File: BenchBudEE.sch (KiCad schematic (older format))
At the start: 0 parts

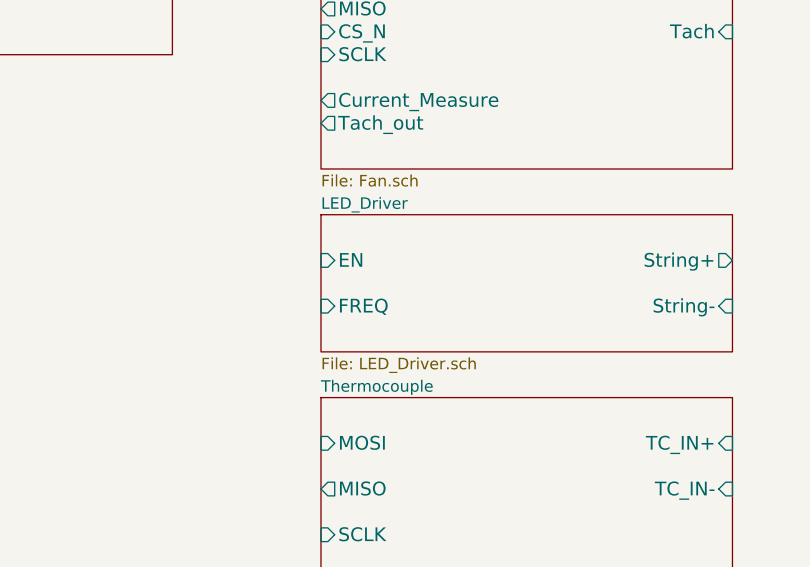
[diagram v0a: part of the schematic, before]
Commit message: Rough schematic created for LED driver circuit
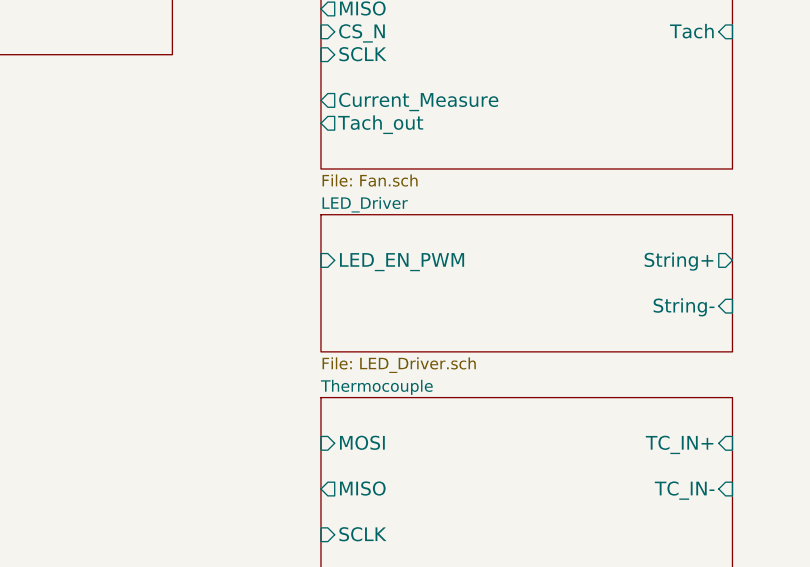
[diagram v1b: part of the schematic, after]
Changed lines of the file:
@@
 F0 "LED_Driver" 50
 F1 "LED_Driver.sch" 50
-F2 "EN" I L 7500 3300 60
-F3 "FREQ" I L 7500 3500 60
-F4 "String+" O R 9300 3300 60
-F5 "String-" I R 9300 3500 60
+F2 "String+" O R 9300 3300 60
+F3 "String-" I R 9300 3500 60
+F4 "LED_EN_PWM" I L 7500 3300 60
 $EndSheet
 $Sheet

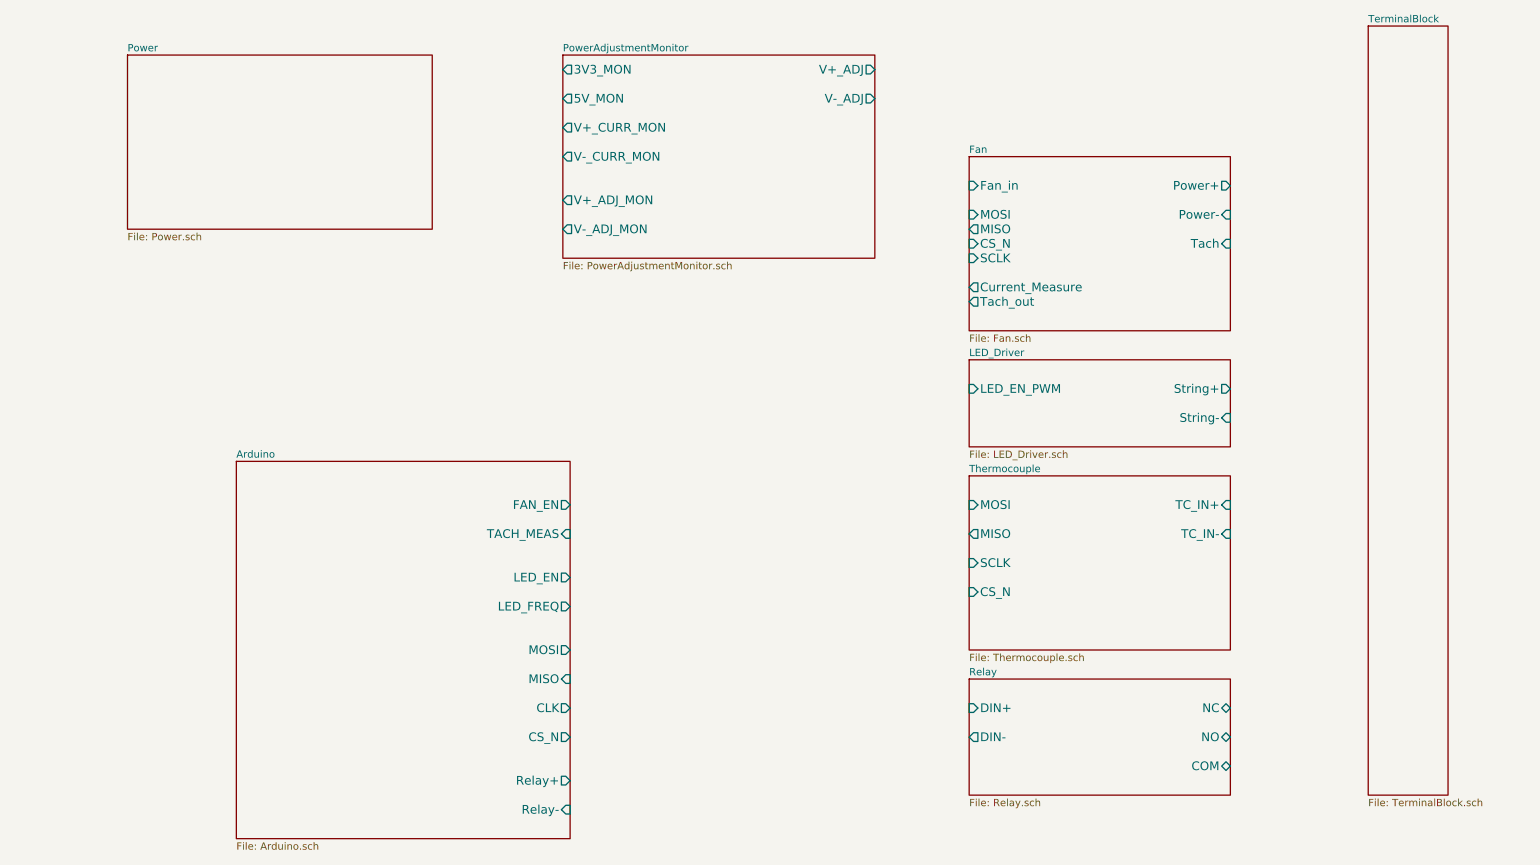
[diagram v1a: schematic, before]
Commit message: Added Arduino and top-level connections
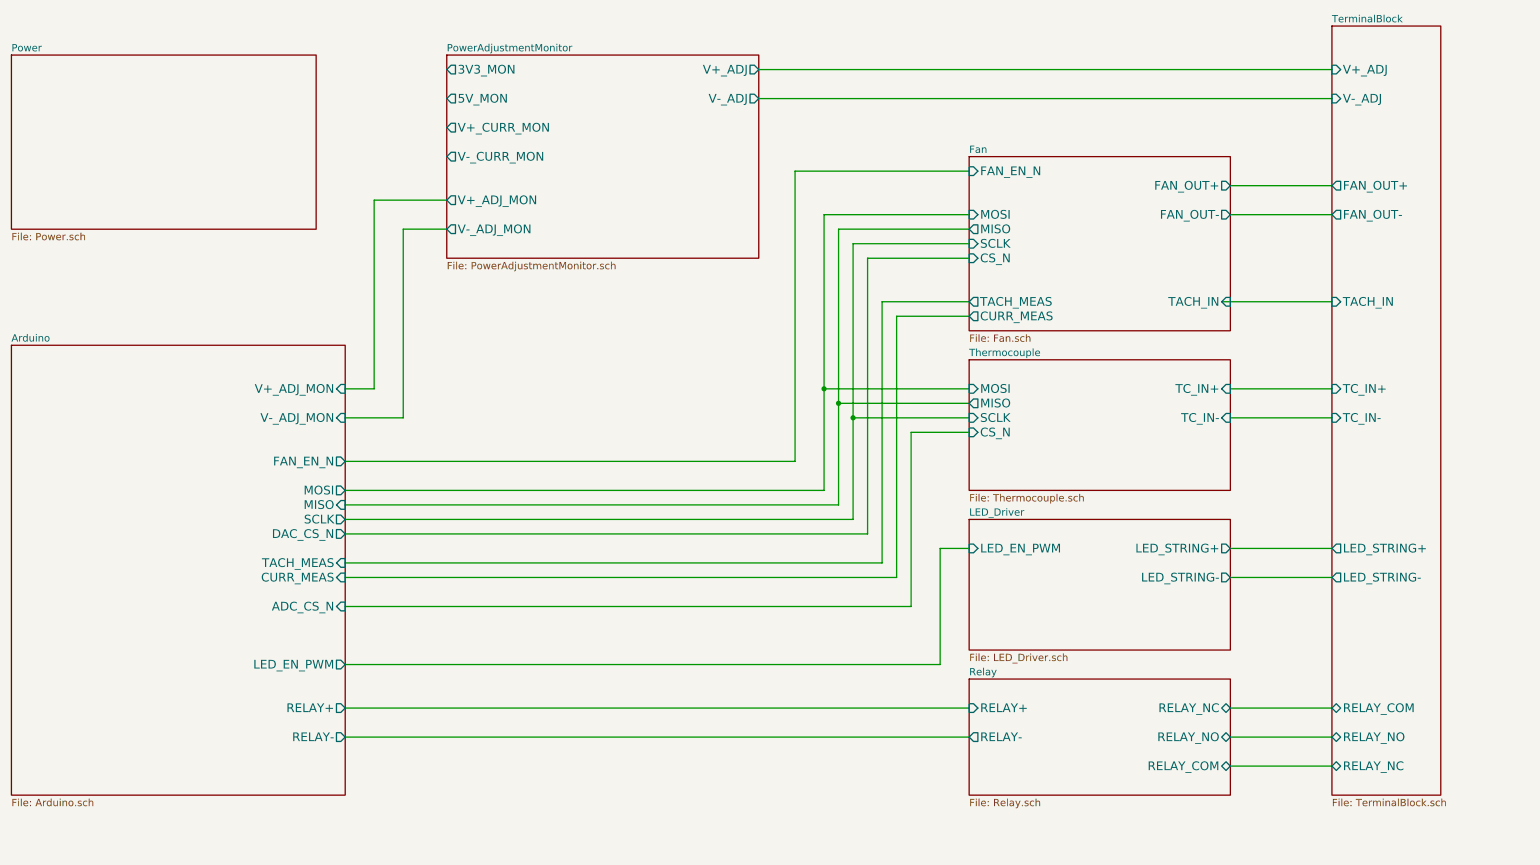
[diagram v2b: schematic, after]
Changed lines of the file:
@@
 $EndDescr
-$Sheet
-S 7500 3900 1800 1200
-U 52EAE493
-F0 "Thermocouple" 50
-F1 "Thermocouple.sch" 50
-F2 "TC_IN+" I R 9300 4100 60
-F3 "TC_IN-" I R 9300 4300 60
-F4 "MOSI" I L 7500 4100 60
-F5 "MISO" O L 7500 4300 60
-F6 "SCLK" I L 7500 4500 60
-F7 "CS_N" I L 7500 4700 60
-$EndSheet
 $Sheet
 S 7500 5300 1800 800
@@
 F0 "Relay" 50
 F1 "Relay.sch" 50
-F2 "DIN+" I L 7500 5500 60
-F3 "DIN-" O L 7500 5700 60
-F4 "NC" B R 9300 5500 60
-F5 "NO" B R 9300 5700 60
-F6 "COM" B R 9300 5900 60
-$EndSheet
-$Sheet
-S 7500 3100 1800 600
+F4 "RELAY_NC" B R 9300 5500 60
+F5 "RELAY_NO" B R 9300 5700 60
+F6 "RELAY_COM" B R 9300 5900 60
+F7 "RELAY+" I L 7500 5500 60
+F8 "RELAY-" O L 7500 5700 60
+$EndSheet
+$Sheet
+S 7500 4200 1800 900
 U 52EAE512
 F0 "LED_Driver" 50
 F1 "LED_Driver.sch" 50
-F2 "String+" O R 9300 3300 60
-F3 "String-" I R 9300 3500 60
-F4 "LED_EN_PWM" I L 7500 3300 60
-$EndSheet
-$Sheet
-S 1700 1000 2100 1200
+F2 "LED_EN_PWM" I L 7500 4400 60
+F3 "LED_STRING+" O R 9300 4400 60
+F4 "LED_STRING-" O R 9300 4600 60
+$EndSheet
+$Sheet
+S 900  1000 2100 1200
 U 52EAE4E0
 F0 "Power" 50
@@
 $EndSheet
 $Sheet
-S 10250 800  550  5300
+S 10000 800  750  5300
 U 52EAE551
 F0 "TerminalBlock" 50
 F1 "TerminalBlock.sch" 50
-$EndSheet
-$Sheet
-S 2450 3800 2300 2600
-U 52EAE42B
-F0 "Arduino" 50
-F1 "Arduino.sch" 50
-F2 "Relay+" O R 4750 6000 60
-F3 "Relay-" I R 4750 6200 60
-F4 "MOSI" O R 4750 5100 60
-F5 "MISO" I R 4750 5300 60
-F6 "CLK" O R 4750 5500 60
-F7 "CS_N" O R 4750 5700 60
-F8 "LED_EN" O R 4750 4600 60
-F9 "LED_FREQ" O R 4750 4800 60
-F10 "FAN_EN" O R 4750 4100 60
-F11 "TACH_MEAS" I R 4750 4300 60
-$EndSheet
+F2 "V+_ADJ" I L 10000 1100 60
+F3 "V-_ADJ" I L 10000 1300 60
+F4 "FAN_OUT+" O L 10000 1900 60
+F5 "FAN_OUT-" O L 10000 2100 60
+F6 "TACH_IN" I L 10000 2700 60
+F7 "LED_STRING+" O L 10000 4400 60
+F8 "LED_STRING-" O L 10000 4600 60
+F9 "TC_IN+" I L 10000 3300 60
+F10 "TC_IN-" I L 10000 3500 60
+F11 "RELAY_COM" B L 10000 5500 60
+F12 "RELAY_NO" B L 10000 5700 60
+F13 "RELAY_NC" B L 10000 5900 60
+$EndSheet
+$Sheet
+S 3900 1000 2150 1400
+U 52F17012
+F0 "PowerAdjustmentMonitor" 50
+F1 "PowerAdjustmentMonitor.sch" 50
+F2 "V+_ADJ" O R 6050 1100 60
+F3 "V-_ADJ" O R 6050 1300 60
+F4 "3V3_MON" O L 3900 1100 60
+F5 "5V_MON" O L 3900 1300 60
+F6 "V+_ADJ_MON" O L 3900 2000 60
+F7 "V-_ADJ_MON" O L 3900 2200 60
+F8 "V+_CURR_MON" O L 3900 1500 60
+F9 "V-_CURR_MON" O L 3900 1700 60
+$EndSheet
+Wire Wire Line
+	10000 1100 6050 1100
+Wire Wire Line
+	10000 1300 6050 1300
+Wire Wire Line
+	10000 1900 9300 1900
+Wire Wire Line
+	10000 2100 9300 2100
+Wire Wire Line
+	9250 2700 10000 2700
+Wire Wire Line
+	10000 3300 9300 3300
+Wire Wire Line
+	10000 3500 9300 3500
+Wire Wire Line
+	10000 4400 9300 4400
+Wire Wire Line
+	10000 4600 9300 4600
+Wire Wire Line
+	10000 5500 9300 5500
+Wire Wire Line
+	10000 5700 9300 5700
+Wire Wire Line
+	10000 5900 9300 5900
+Wire Wire Line
+	3200 3300 3400 3300
+Wire Wire Line
+	3400 3300 3400 2000
+Wire Wire Line
+	3400 2000 3900 2000
+Wire Wire Line
+	3200 3500 3600 3500
+Wire Wire Line
+	3600 3500 3600 2200
+Wire Wire Line
+	3600 2200 3900 2200
+Wire Wire Line
+	3200 3800 6300 3800
+Wire Wire Line
+	6300 3800 6300 1800
+Wire Wire Line
+	6300 1800 7500 1800
+Wire Wire Line
+	6500 4000 3200 4000
+Wire Wire Line
+	6500 2100 6500 4000
+Wire Wire Line
+	6500 2100 7500 2100
+Wire Wire Line
+	6600 4100 3200 4100
+Wire Wire Line
+	6600 2200 6600 4100
+Wire Wire Line
+	6600 2200 7500 2200
+Wire Wire Line
+	6700 4200 3200 4200
+Wire Wire Line
+	6700 2300 6700 4200
+Wire Wire Line
+	6700 2300 7500 2300
+Wire Wire Line
+	3200 4300 6800 4300
+Wire Wire Line
+	6800 4300 6800 2400
+Wire Wire Line
+	6800 2400 7500 2400
+Wire Wire Line
+	3200 4500 6900 4500
+Wire Wire Line
+	6900 4500 6900 2700
+Wire Wire Line
+	6900 2700 7500 2700
+Wire Wire Line
+	3200 4600 7000 4600
+Wire Wire Line
+	7000 4600 7000 2800
+Wire Wire Line
+	7000 2800 7500 2800
 $Sheet
 S 7500 1700 1800 1200
@@
 F0 "Fan" 50
 F1 "Fan.sch" 50
-F2 "Power+" O R 9300 1900 60
-F3 "Power-" I R 9300 2100 60
-F4 "Tach" I R 9300 2300 60
-F5 "Tach_out" O L 7500 2700 60
-F6 "Fan_in" I L 7500 1900 60
-F7 "Current_Measure" O L 7500 2600 60
-F8 "MOSI" I L 7500 2100 60
-F9 "MISO" O L 7500 2200 60
-F10 "CS_N" I L 7500 2300 60
-F11 "SCLK" I L 7500 2400 60
-$EndSheet
-$Sheet
-S 4700 1000 2150 1400
-U 52F17012
-F0 "PowerAdjustmentMonitor" 50
-F1 "PowerAdjustmentMonitor.sch" 50
-F2 "V+_ADJ" O R 6850 1100 60
-F3 "V-_ADJ" O R 6850 1300 60
-F4 "3V3_MON" O L 4700 1100 60
-F5 "5V_MON" O L 4700 1300 60
-F6 "V+_ADJ_MON" O L 4700 2000 60
-F7 "V-_ADJ_MON" O L 4700 2200 60
-F8 "V+_CURR_MON" O L 4700 1500 60
-F9 "V-_CURR_MON" O L 4700 1700 60
-$EndSheet
+F2 "MOSI" I L 7500 2100 60
+F3 "MISO" O L 7500 2200 60
+F4 "CS_N" I L 7500 2400 60
+F5 "SCLK" I L 7500 2300 60
+F6 "FAN_OUT+" O R 9300 1900 60
+F7 "TACH_IN" I R 9300 2700 60
+F8 "TACH_MEAS" O L 7500 2700 60
+F9 "FAN_EN_N" I L 7500 1800 60
+F10 "CURR_MEAS" O L 7500 2800 60
+F11 "FAN_OUT-" O R 9300 2100 60
+$EndSheet
+$Sheet
+S 7500 3100 1800 900
+U 52EAE493
+F0 "Thermocouple" 50
+F1 "Thermocouple.sch" 50
+F2 "TC_IN+" I R 9300 3300 60
+F3 "TC_IN-" I R 9300 3500 60
+F4 "MOSI" I L 7500 3300 60
+F5 "MISO" O L 7500 3400 60
+F6 "SCLK" I L 7500 3500 60
+F7 "CS_N" I L 7500 3600 60
+$EndSheet
+$Sheet
+S 900  3000 2300 3100
+U 52EAE42B
+F0 "Arduino" 50
+F1 "Arduino.sch" 50
+F2 "MOSI" O R 3200 4000 60
+F3 "MISO" I R 3200 4100 60
+F4 "TACH_MEAS" I R 3200 4500 60
+F5 "SCLK" O R 3200 4200 60
+F6 "FAN_EN_N" O R 3200 3800 60
+F7 "CURR_MEAS" I R 3200 4600 60
+F8 "RELAY+" O R 3200 5500 60
+F9 "RELAY-" O R 3200 5700 60
+F10 "V+_ADJ_MON" I R 3200 3300 60
+F11 "V-_ADJ_MON" I R 3200 3500 60
+F12 "LED_EN_PWM" O R 3200 5200 60
+F13 "DAC_CS_N" O R 3200 4300 60
+F14 "ADC_CS_N" I R 3200 4800 60
+$EndSheet
+Wire Wire Line
+	3200 4800 7100 4800
+Wire Wire Line
+	7100 4800 7100 3600
+Wire Wire Line
+	7100 3600 7500 3600
+Wire Wire Line
+	7500 3500 6700 3500
+Connection ~ 6700 3500
+Wire Wire Line
+	7500 3400 6600 3400
+Connection ~ 6600 3400
+Wire Wire Line
+	7500 3300 6500 3300
+Connection ~ 6500 3300
+Wire Wire Line
+	3200 5200 7300 5200
+Wire Wire Line
+	7300 5200 7300 4400
+Wire Wire Line
+	7300 4400 7500 4400
+Wire Wire Line
+	3200 5500 7500 5500
+Wire Wire Line
+	7500 5700 3200 5700
 $EndSCHEMATC

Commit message: Some cleanup/fixes on the top-level
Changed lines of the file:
@@
 	10000 5900 9300 5900
 Wire Wire Line
-	3200 3300 3400 3300
+	3200 3200 3400 3200
 Wire Wire Line
-	3400 3300 3400 2000
+	3400 3200 3400 2000
 Wire Wire Line
 	3400 2000 3900 2000
 Wire Wire Line
-	3200 3500 3600 3500
+	3200 3400 3600 3400
 Wire Wire Line
-	3600 3500 3600 2200
+	3600 3400 3600 2200
 Wire Wire Line
 	3600 2200 3900 2200
@@
 	3200 3800 6300 3800
 Wire Wire Line
-	6300 3800 6300 1800
+	6300 3800 6300 1900
 Wire Wire Line
-	6300 1800 7500 1800
+	6300 1900 7500 1900
 Wire Wire Line
 	6500 4000 3200 4000
 Wire Wire Line
-	6500 2100 6500 4000
+	6500 2100 6500 3300
+Wire Wire Line
+	6500 3300 6500 4000
 Wire Wire Line
 	6500 2100 7500 2100
@@
 	6600 4100 3200 4100
 Wire Wire Line
-	6600 2200 6600 4100
+	6600 2200 6600 3400
+Wire Wire Line
+	6600 3400 6600 4100
 Wire Wire Line
 	6600 2200 7500 2200
@@
 	6700 4200 3200 4200
 Wire Wire Line
-	6700 2300 6700 4200
+	6700 2300 6700 3500
+Wire Wire Line
+	6700 3500 6700 4200
 Wire Wire Line
 	6700 2300 7500 2300
@@
 F7 "TACH_IN" I R 9300 2700 60
 F8 "TACH_MEAS" O L 7500 2700 60
-F9 "FAN_EN_N" I L 7500 1800 60
-F10 "CURR_MEAS" O L 7500 2800 60
-F11 "FAN_OUT-" O R 9300 2100 60
+F9 "CURR_MEAS" O L 7500 2800 60
+F10 "FAN_OUT-" O R 9300 2100 60
+F11 "FAN_PWM" I L 7500 1900 60
+F12 "FAN_MODE" I L 7500 1800 60
 $EndSheet
 $Sheet
@@
 F4 "TACH_MEAS" I R 3200 4500 60
 F5 "SCLK" O R 3200 4200 60
-F6 "FAN_EN_N" O R 3200 3800 60
-F7 "CURR_MEAS" I R 3200 4600 60
-F8 "RELAY+" O R 3200 5500 60
-F9 "RELAY-" O R 3200 5700 60
-F10 "V+_ADJ_MON" I R 3200 3300 60
-F11 "V-_ADJ_MON" I R 3200 3500 60
-F12 "LED_EN_PWM" O R 3200 5200 60
-F13 "DAC_CS_N" O R 3200 4300 60
-F14 "ADC_CS_N" I R 3200 4800 60
+F6 "CURR_MEAS" I R 3200 4600 60
+F7 "RELAY+" O R 3200 5500 60
+F8 "RELAY-" O R 3200 5700 60
+F9 "V+_ADJ_MON" I R 3200 3200 60
+F10 "V-_ADJ_MON" I R 3200 3400 60
+F11 "LED_EN_PWM" O R 3200 5200 60
+F12 "DAC_CS_N" O R 3200 4300 60
+F13 "ADC_CS_N" I R 3200 4800 60
+F14 "FAN_PWM" O R 3200 3800 60
+F15 "FAN_MODE" I R 3200 3700 60
 $EndSheet
 Wire Wire Line
@@
 Wire Wire Line
 	7500 5700 3200 5700
+Wire Wire Line
+	7500 1800 6200 1800
+Wire Wire Line
+	6200 1800 6200 3700
+Wire Wire Line
+	6200 3700 3200 3700
 $EndSCHEMATC

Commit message: Added footprints for the relay module, preliminarily annotated schematic, relay components placed on PCB
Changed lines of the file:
@@
 	6500 4000 3200 4000
 Wire Wire Line
-	6500 2100 6500 3300
-Wire Wire Line
-	6500 3300 6500 4000
+	6500 2100 6500 4000
 Wire Wire Line
 	6500 2100 7500 2100
@@
 	6600 4100 3200 4100
 Wire Wire Line
-	6600 2200 6600 3400
-Wire Wire Line
-	6600 3400 6600 4100
+	6600 2200 6600 4100
 Wire Wire Line
 	6600 2200 7500 2200
@@
 	6700 4200 3200 4200
 Wire Wire Line
-	6700 2300 6700 3500
-Wire Wire Line
-	6700 3500 6700 4200
+	6700 2300 6700 4200
 Wire Wire Line
 	6700 2300 7500 2300
